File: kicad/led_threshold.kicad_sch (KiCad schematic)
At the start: 16 parts, among them Q1 2N7002E, Q2 2N7002E, SW5 SW_DP3T, U21 OPA189, U22 4x Comparator

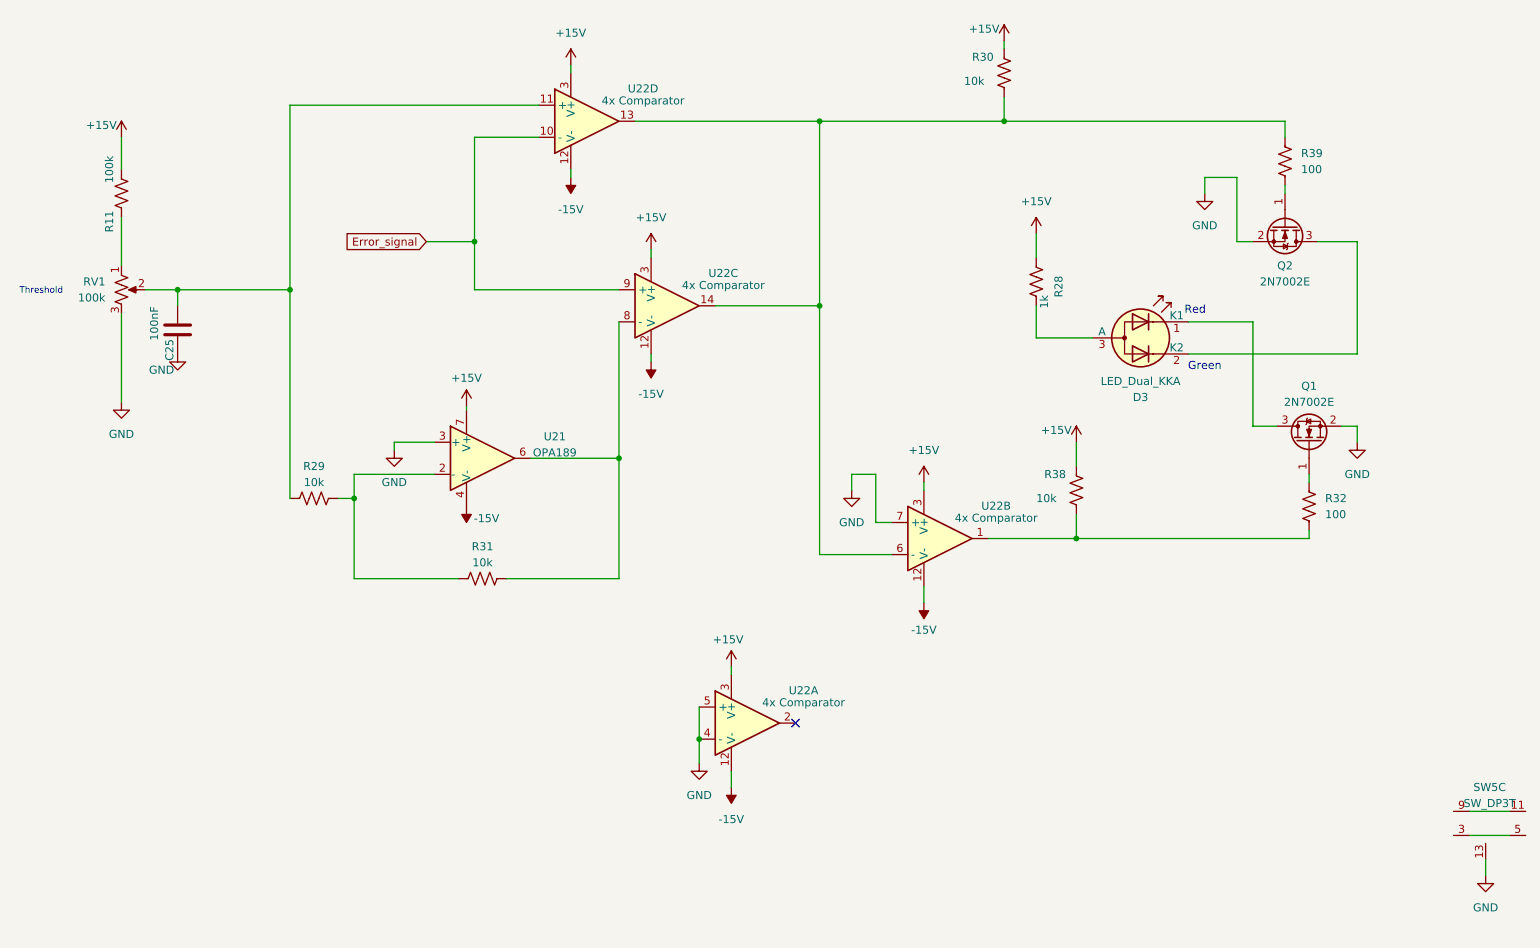
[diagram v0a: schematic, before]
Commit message: First pass at updated schematic and loose PCB grouping, TODO: Fix PI Gain values
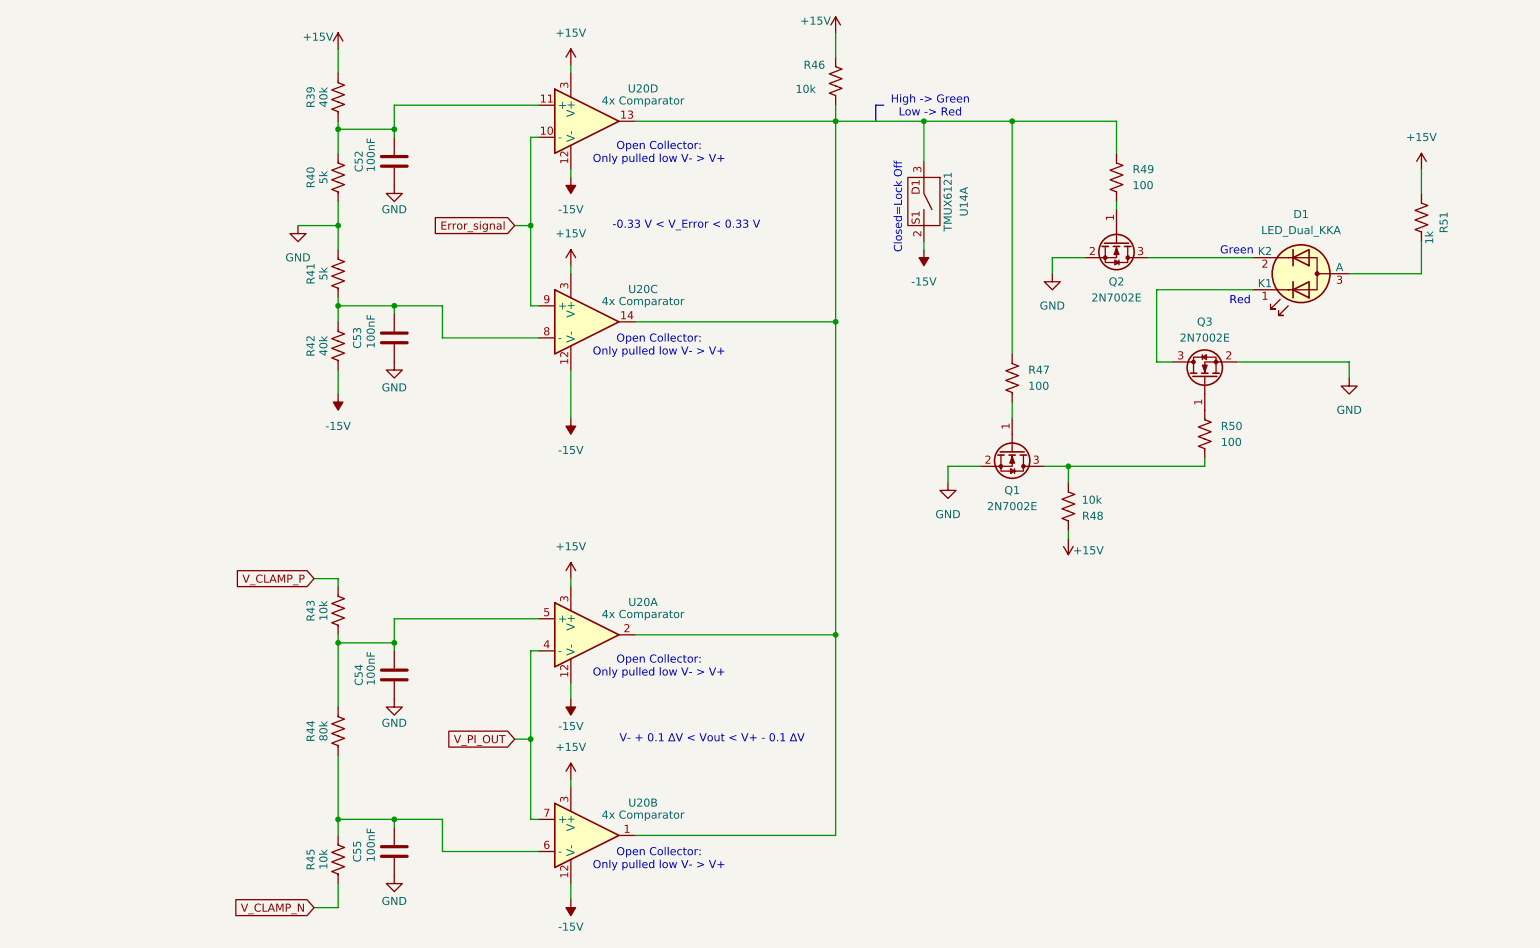
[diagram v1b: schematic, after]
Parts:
- removed R28: 1k, Resistor_SMD:R_0805_2012Metric, symbol Device:R_US
- removed R29, R31, R38: 10k, Resistor_SMD:R_0805_2012Metric, symbol Device:R_US
- removed RV1: 100k, Potentiometer_THT:Potentiometer_Bourns_3296W_Vertical, symbol Device:R_Potentiometer_US
- removed SW5: SW_DP3T, Custom_Footprints:Right Angle 3PDT Switch, symbol Custom_Symbols:DP3T_1
- removed U21: OPA189, Package_SO:SOIC-8_3.9x4.9mm_P1.27mm, symbol Amplifier_Operational:OPA330xxD
- added C52, C54, C55: 100nF, Capacitor_SMD:C_0805_2012Metric, symbol Device:C
- added Q1: 2N7002E, Package_TO_SOT_SMD:SOT-23, symbol Transistor_FET:2N7002E
- added R39, R42: 40k, Resistor_SMD:R_0805_2012Metric, symbol Device:R_US
- added R41: 5k, Resistor_SMD:R_0805_2012Metric, symbol Device:R_US
- added R43, R45, R48: 10k, Resistor_SMD:R_0805_2012Metric, symbol Device:R_US
- added R44: 80k, Resistor_SMD:R_0805_2012Metric, symbol Device:R_US
- added R47: 100, Resistor_SMD:R_0805_2012Metric, symbol Device:R_US
- added R51: 1k, Resistor_SMD:R_0805_2012Metric, symbol Device:R_US
- added U14: TMUX6121, Custom_Footprints:TMUX6121, symbol library_intensity_pi:TMUX6123_split
- R40: renamed from R11; value 100k -> 5k; DIGIKEY P100KDACT-ND -> (none); PARTNO ERA-6AEB104V -> (none)
- renumbered C25 to C53, D3 to D1, Q1 to Q3, R30 to R46, R39 to R49, R32 to R50, U22 to U20
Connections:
- net +15V: now also R39.2, R48.2, R51.1; no longer R40.2
- net -15V: now also R42.1, U14.2
- net GND: now also R40.1, C52.1, C54.1, C55.1, Q1.2 (S), R41.2; no longer U20.4 (-), U20.5 (+), U20.7 (+)
- net at U20.1: now also R46.1, R49.1, U20.13, U20.14, U20.2, R47.1, U14.3; no longer R50.2
- net at U20.11 (+): now also R40.2, C52.2, R39.1; no longer C53.2
- net at U20.8 (-): now also C53.2, R41.1, R42.2
- net at D1.3 (A): now also R51.2
- new net: Q1.1 (G), R47.2
- new net: C55.2, R44.1, R45.2, U20.6 (-)
- new net: C54.2, R43.1, R44.2, U20.5 (+)
- new net: Q1.3 (D), R48.1, R50.2
- new net V_CLAMP_N: R45.1
- new net V_CLAMP_P: R43.2
- new net V_PI_OUT: U20.4 (-), U20.7 (+)
- no-connect marks 1 -> 0
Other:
- note added: "-0.33 V < V_Error < 0.33 V"
- note added: "Closed=Lock Off"
- note added: "High -> Green Low -> Red"
- note added: "Open Collector: Only pulled low V- > V+"
- note added: "V- + 0.1 ∆V < Vout < V+ - 0.1 ∆V"
- note removed: "Threshold"
- moved on the sheet: C53, D1, Q2, Q3, R40, R46, R49, R50, U20A, U20B, U20C
